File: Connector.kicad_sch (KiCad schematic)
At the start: 7 parts, among them J1 1-1376430-0

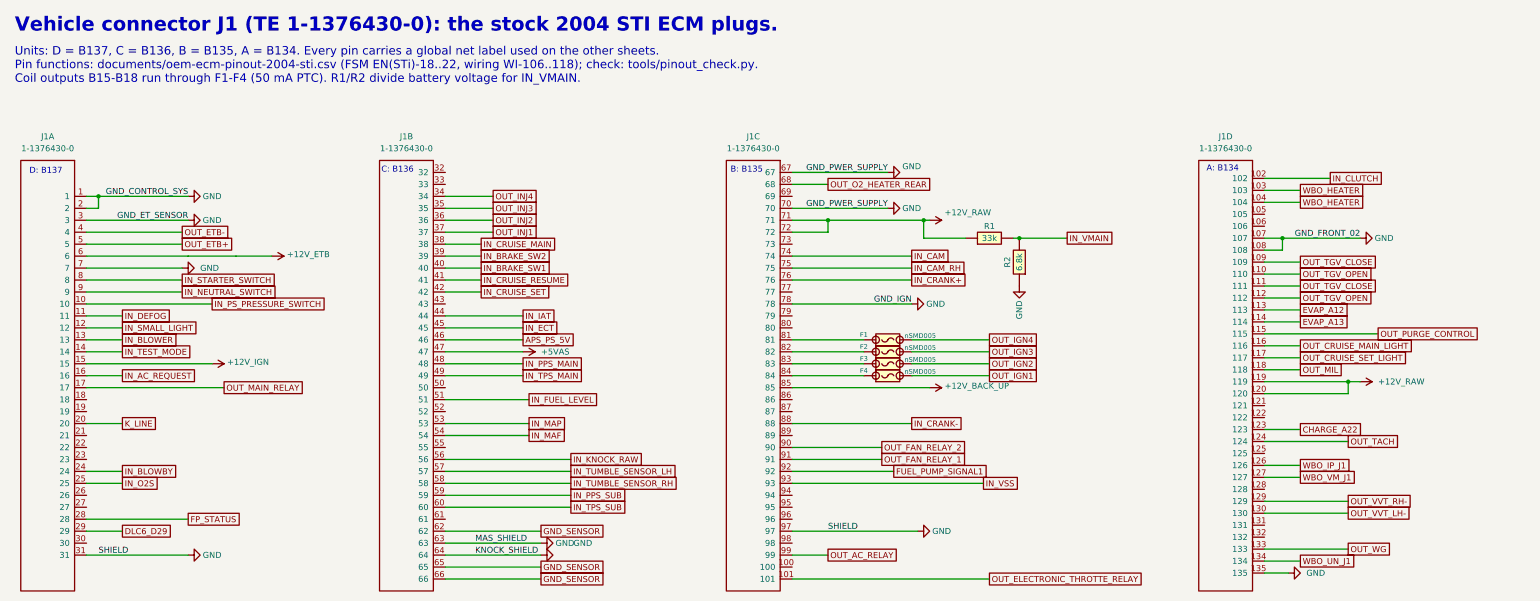
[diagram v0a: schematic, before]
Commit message: EmbeddedEra libraries and template, KiCad 10
- Every symbol except the nine Hellen-One modules now comes from the EmbeddedEra library (resistors and 0R links from the generic libraries, PTC fuses, VND14NV04-E, TE 1-1376430-0, Molex 39281143, test pads, proto area, power symbols). Same-pin parts swapped in place; resistors re-placed between their old pin points with short wires. New parts live on library branch sti2004-parts.
- EmbeddedEra project template: worksheet, text variables, net classes with explicit power classes, JLCPCB design rules; template net names for USB, I2C and the K-line UART.
- Migrated all sheets and the board to KiCad 10 (10.0.7).
- tools/sch_overlap_check.py also fails on overlapping symbol bodies and on fields printed across a wire (found the stacked PTC fuses); KiCad 10 hide flags understood.

Verified: connectivity identical to the previous commit (167 nets), only the planned net renames; 0 overlaps on all 10 sheet files; ERC errors unchanged (148); pinout check 99 OK.

Co-Authored-By: Claude Opus 5.5 <noreply@anthropic.com>
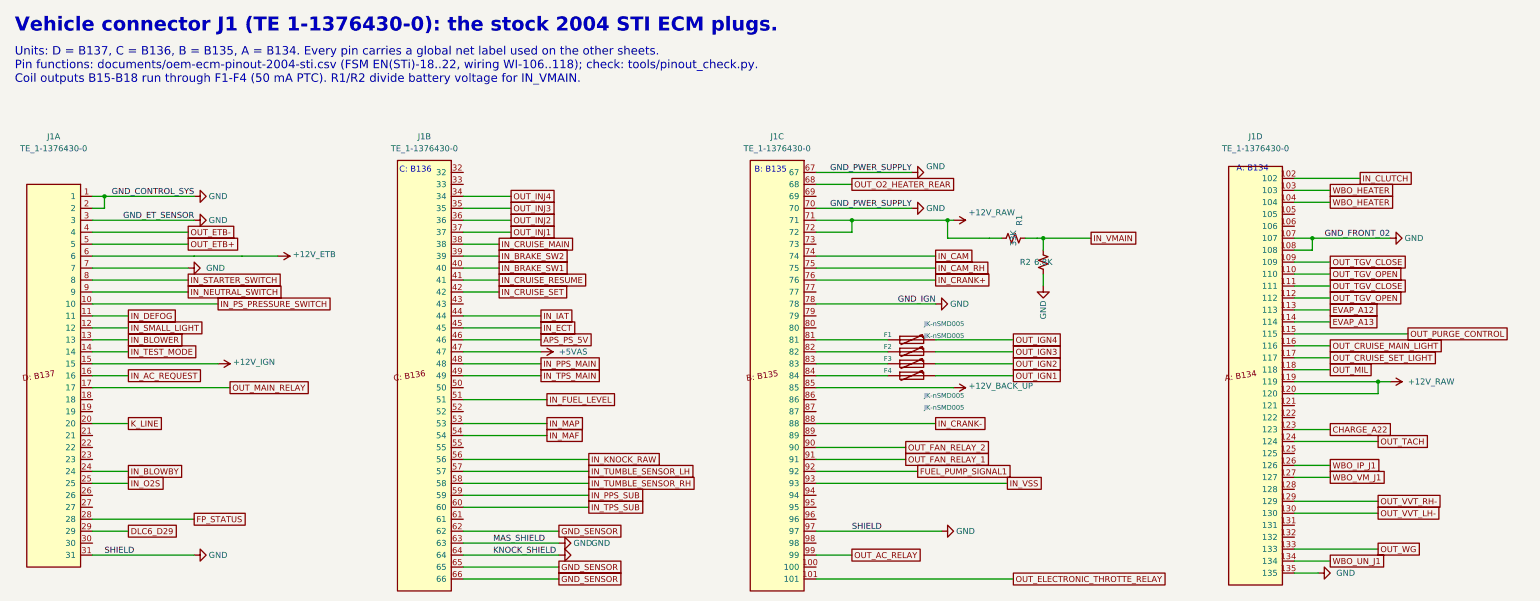
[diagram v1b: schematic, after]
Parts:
- F1, F2, F3, F4: value nSMD005 -> JK-nSMD005; footprint hellen-one-common:PAD-1206-PAD -> EmbeddedEra_Library:Fuse_1206_3216Metric; symbol hellen-one-common:Fuse-Pad-Pad -> EmbeddedEra:JK-nSMD005; Manufacturer (none) -> Jinrui; Manufacturer Part Number (none) -> JK-nSMD005
- J1: value 1-1376430-0 -> TE_1-1376430-0; footprint STI:1-1376430-0 -> EmbeddedEra_Library:TE_1-1376430-0; symbol rusefi_1-1376430-0_135pin:1-1376430-0 -> EmbeddedEra:TE_1-1376430-0; Manufacturer (none) -> TE Connectivity; Manufacturer Part Number (none) -> 1-1376430-0
- R1: value 33k -> 33K; footprint hellen-one-common:R0603 -> EmbeddedEra_Library:R_0603_1608Metric; symbol hellen-one-common:Res -> EmbeddedEra_Resistors_0603:EE_R_0603_33K_1%; LCSC C4216 -> C126359; Manufacturer (none) -> YAGEO; Manufacturer Part Number (none) -> RC0603FR-0733KL
- R2: value 6.8k -> 6.8K; footprint hellen-one-common:R0603 -> EmbeddedEra_Library:R_0603_1608Metric; symbol hellen-one-common:Res -> EmbeddedEra_Resistors_0603:EE_R_0603_6.8K_1%; LCSC C23212 -> C114632; Manufacturer (none) -> YAGEO; Manufacturer Part Number (none) -> RC0603FR-076K8L
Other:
- note removed: "D: B137"
- moved on the sheet: R1, R2
